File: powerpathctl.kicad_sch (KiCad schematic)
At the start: 11 parts, among them J10 Conn_01x06_Male, J11 Conn_01x06_Male_BAT_data, J8 Conn_01x03_Male_BAT_PWR_IN_NU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, J9 Conn_01x03_Male_BAT_PWR, Q1 SI7149ADP-T1-GE3, U7 LTC4412ES6

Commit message: fixed component number and url for the 5.1kOhm USB pulldown resistors
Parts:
- R20: renamed from R?; footprint (none) -> Resistor_SMD:R_0603_1608Metric; LCSC Part (none) -> C4216
- R21: renamed from R?; footprint (none) -> Resistor_SMD:R_0603_1608Metric; LCSC Part (none) -> C25811
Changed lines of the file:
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@@
   (symbol (lib_id "Device:R") (at 110.7948 81.4832 180) (unit 1)
     (in_bom yes) (on_board yes) (fields_autoplaced)
-    (property "Reference" "R?" (id 0) (at 113.3856 80.2131 0)
+    (property "Reference" "R20" (id 0) (at 113.3856 80.2131 0)
       (effects (font (size 1.27 1.27)) (justify right))
     )
@@
       (effects (font (size 1.27 1.27)) (justify right))
     )
-    (property "Footprint" "" (id 2) (at 112.5728 81.4832 90))
-    (property "Datasheet" "~" (id 3) (at 110.7948 81.4832 0)
+    (property "Footprint" "Resistor_SMD:R_0603_1608Metric" (id 2) (at 112.5728 81.4832 90)
+      (effects (font (size 1.27 1.27)) hide)
+    )
+    (property "Datasheet" "https://datasheet.lcsc.com/lcsc/2206010230_UNI-ROYAL-Uniroyal-Elec-0603WAF3302T5E_C4216.pdf" (id 3) (at 110.7948 81.4832 0)
+      (effects (font (size 1.27 1.27)) hide)
+    )
+    (property "LCSC Part" "C4216" (id 4) (at 110.7948 81.4832 0)
       (effects (font (size 1.27 1.27)) hide)
     )
@@
   (symbol (lib_id "power:GND") (at 110.871 97.4852 0) (unit 1)
     (in_bom yes) (on_board yes) (fields_autoplaced)
-    (property "Reference" "#PWR?" (id 0) (at 110.871 103.8352 0)
+    (property "Reference" "#PWR0131" (id 0) (at 110.871 103.8352 0)
       (effects (font (size 1.27 1.27)) hide)
     )
@@
   (symbol (lib_id "Device:R") (at 110.871 93.0402 0) (unit 1)
     (in_bom yes) (on_board yes) (fields_autoplaced)
-    (property "Reference" "R?" (id 0) (at 113.5126 91.7701 0)
+    (property "Reference" "R21" (id 0) (at 113.5126 91.7701 0)
       (effects (font (size 1.27 1.27)) (justify left))
     )
@@
       (effects (font (size 1.27 1.27)) (justify left))
     )
-    (property "Footprint" "" (id 2) (at 109.093 93.0402 90))
-    (property "Datasheet" "~" (id 3) (at 110.871 93.0402 0)
-      (effects (font (size 1.27 1.27)) hide)
-    )
+    (property "Footprint" "Resistor_SMD:R_0603_1608Metric" (id 2) (at 109.093 93.0402 90)
+      (effects (font (size 1.27 1.27)) hide)
+    )
+    (property "Datasheet" "https://datasheet.lcsc.com/lcsc/2206010045_UNI-ROYAL-Uniroyal-Elec-0603WAF2003T5E_C25811.pdf" (id 3) (at 110.871 93.0402 0)
+      (effects (font (size 1.27 1.27)) hide)
+    )
+    (property "LCSC Part" "C25811" (id 4) (at 110.871 93.0402 0)
+      (effects (font (size 1.27 1.27)) hide)
+    )

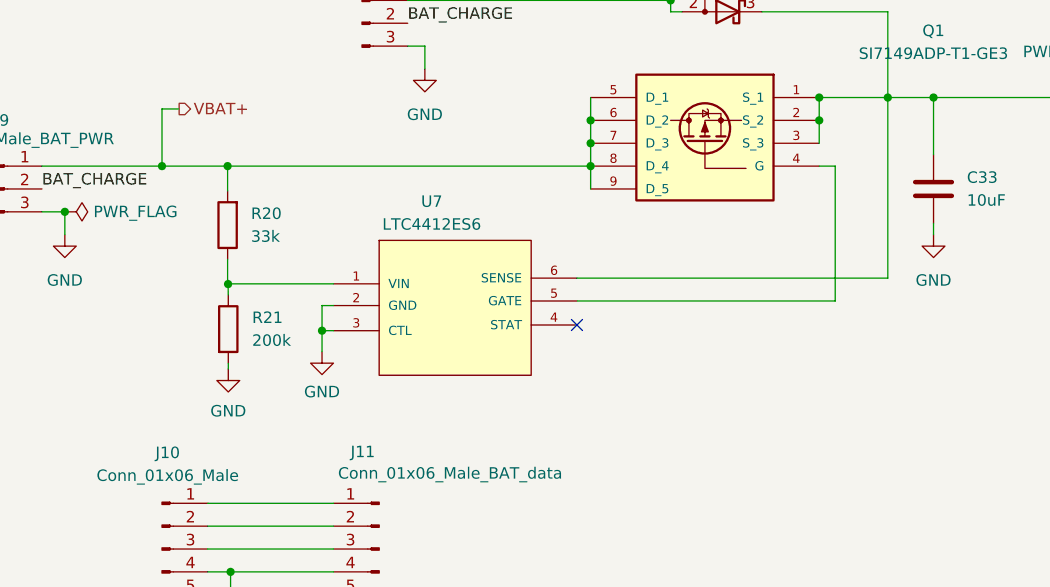
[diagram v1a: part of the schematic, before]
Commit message: updated pcb from schematics, rerouted M1 enc GND and VCC, placed powerpathctl voltage divider
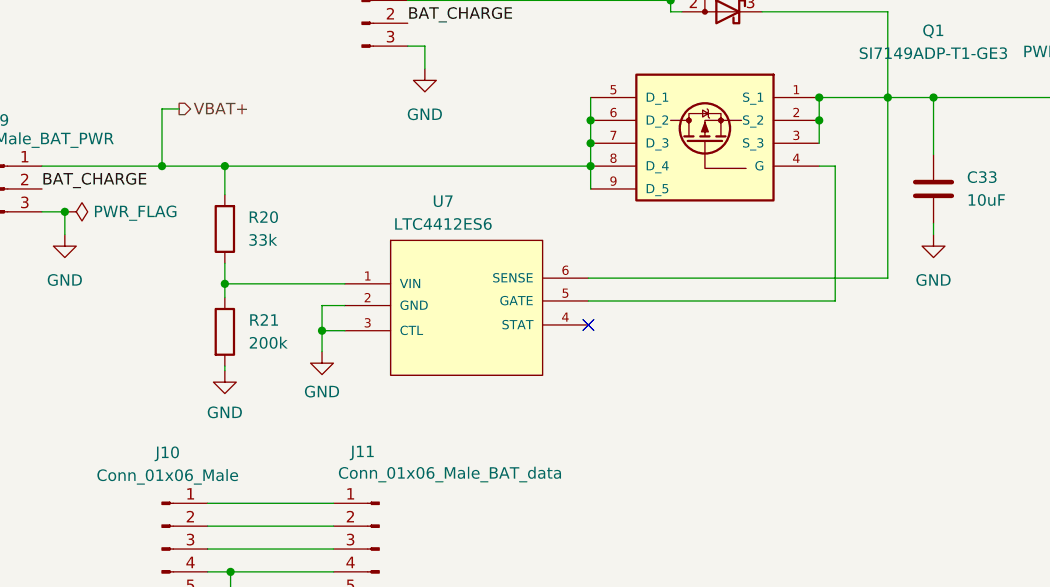
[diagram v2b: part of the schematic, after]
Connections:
- net at R20.1, U7.1 (VIN): now also R21.1
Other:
- moved on the sheet: R20, U7
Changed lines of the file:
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@@
   (junction (at 203.835 67.31) (diameter 0) (color 0 0 0 0)
   )
-  (junction (at 110.7948 74.93) (diameter 0) (color 0 0 0 0)
+  (junction (at 110.49 74.93) (diameter 0) (color 0 0 0 0)
   )
   (junction (at 151.13 74.93) (diameter 0) (color 0 0 0 0)
@@
   (junction (at 103.505 74.93) (diameter 0) (color 0 0 0 0)
   )
+  (junction (at 110.49 88.011) (diameter 0) (color 0 0 0 0)
+  )
   (junction (at 92.71 80.01) (diameter 0) (color 0 0 0 0)
   )
   (junction (at 151.13 72.39) (diameter 0) (color 0 0 0 0)
   )
-  (junction (at 110.8456 88.0364) (diameter 0) (color 0 0 0 0)
-  )
   (junction (at 184.15 67.31) (diameter 0) (color 0 0 0 0)
   )
-  (no_connect (at 149.606 92.583))
+  (no_connect (at 150.876 92.583))
   (wire (pts (xy 132.715 61.595) (xy 132.715 64.135))
     (stroke (width 0) (type default) (color 0 0 0 0))
   )
-  (wire (pts (xy 110.7948 74.93) (xy 151.13 74.93))
+  (wire (pts (xy 110.49 74.93) (xy 151.13 74.93))
     (stroke (width 0) (type default) (color 0 0 0 0))
   )
@@
     (stroke (width 0) (type default) (color 0 0 0 0))
   )
+  (wire (pts (xy 110.49 88.011) (xy 110.49 89.535))
+    (stroke (width 0) (type default) (color 0 0 0 0))
+  )
   (wire (pts (xy 108.585 117.475) (xy 122.555 117.475))
     (stroke (width 0) (type default) (color 0 0 0 0))
@@
     (stroke (width 0) (type default) (color 0 0 0 0))
   )
+  (wire (pts (xy 110.49 88.011) (xy 123.825 88.011))
+    (stroke (width 0) (type default) (color 0 0 0 0))
+  )
   (wire (pts (xy 121.285 90.424) (xy 121.285 93.218))
     (stroke (width 0) (type default) (color 0 0 0 0))
@@
     (stroke (width 0) (type default) (color 0 0 0 0))
   )
-  (wire (pts (xy 149.606 89.916) (xy 178.308 89.916))
-    (stroke (width 0) (type default) (color 0 0 0 0))
-  )
-  (wire (pts (xy 121.285 93.218) (xy 122.555 93.218))
+  (wire (pts (xy 150.876 89.916) (xy 178.308 89.916))
+    (stroke (width 0) (type default) (color 0 0 0 0))
+  )
+  (wire (pts (xy 121.285 93.218) (xy 123.825 93.218))
     (stroke (width 0) (type default) (color 0 0 0 0))
   )
@@
     (stroke (width 0) (type default) (color 0 0 0 0))
   )
-  (wire (pts (xy 110.871 96.8502) (xy 110.871 97.4852))
+  (wire (pts (xy 110.49 97.155) (xy 110.49 97.663))
     (stroke (width 0) (type default) (color 0 0 0 0))
   )
@@
     (stroke (width 0) (type default) (color 0 0 0 0))
   )
-  (wire (pts (xy 122.555 90.424) (xy 121.285 90.424))
+  (wire (pts (xy 123.825 90.424) (xy 121.285 90.424))
     (stroke (width 0) (type default) (color 0 0 0 0))
   )
@@
     (stroke (width 0) (type default) (color 0 0 0 0))
   )
-  (wire (pts (xy 110.871 89.2302) (xy 110.8456 88.0364))
-    (stroke (width 0) (type default) (color 0 0 0 0))
-  )
   (wire (pts (xy 111.125 130.175) (xy 113.03 130.175))
     (stroke (width 0) (type default) (color 0 0 0 0))
@@
     (stroke (width 0) (type default) (color 0 0 0 0))
   )
-  (wire (pts (xy 149.606 87.376) (xy 184.15 87.376))
+  (wire (pts (xy 150.876 87.376) (xy 184.15 87.376))
     (stroke (width 0) (type default) (color 0 0 0 0))
   )
@@
     (stroke (width 0) (type default) (color 0 0 0 0))
   )
-  (wire (pts (xy 103.505 74.93) (xy 110.7948 74.93))
+  (wire (pts (xy 103.505 74.93) (xy 110.49 74.93))
     (stroke (width 0) (type default) (color 0 0 0 0))
   )
@@
     (stroke (width 0) (type default) (color 0 0 0 0))
   )
-  (wire (pts (xy 110.7948 74.93) (xy 110.7948 77.6732))
+  (wire (pts (xy 110.49 74.93) (xy 110.49 78.105))
     (stroke (width 0) (type default) (color 0 0 0 0))
   )
@@
     (stroke (width 0) (type default) (color 0 0 0 0))
   )
-  (wire (pts (xy 110.7948 85.2932) (xy 110.7948 88.011))
-    (stroke (width 0) (type default) (color 0 0 0 0))
-  )
   (wire (pts (xy 111.125 120.015) (xy 111.125 130.175))
     (stroke (width 0) (type default) (color 0 0 0 0))
   )
-  (wire (pts (xy 110.7948 88.011) (xy 122.555 88.011))
+  (wire (pts (xy 110.49 85.725) (xy 110.49 88.011))
     (stroke (width 0) (type default) (color 0 0 0 0))
   )
@@
     (pin "3")
   )
-  (symbol (lib_id "Device:R") (at 110.7948 81.4832 180) (unit 1)
-    (in_bom yes) (on_board yes) (fields_autoplaced)
-    (property "Reference" "R20" (id 0) (at 113.3856 80.2131 0)
+  (symbol (lib_id "Device:R") (at 110.49 81.915 180) (unit 1)
+    (in_bom yes) (on_board yes) (fields_autoplaced)
+    (property "Reference" "R20" (id 0) (at 113.0808 80.6449 0)
       (effects (font (size 1.27 1.27)) (justify right))
     )
-    (property "Value" "33k" (id 1) (at 113.3856 82.7531 0)
+    (property "Value" "33k" (id 1) (at 113.0808 83.1849 0)
       (effects (font (size 1.27 1.27)) (justify right))
     )
-    (property "Footprint" "Resistor_SMD:R_0603_1608Metric" (id 2) (at 112.5728 81.4832 90)
-      (effects (font (size 1.27 1.27)) hide)
-    )
-    (property "Datasheet" "https://datasheet.lcsc.com/lcsc/2206010230_UNI-ROYAL-Uniroyal-Elec-0603WAF3302T5E_C4216.pdf" (id 3) (at 110.7948 81.4832 0)
-      (effects (font (size 1.27 1.27)) hide)
-    )
-    (property "LCSC Part" "C4216" (id 4) (at 110.7948 81.4832 0)
+    (property "Footprint" "Resistor_SMD:R_0603_1608Metric" (id 2) (at 112.268 81.915 90)
+      (effects (font (size 1.27 1.27)) hide)
+    )
+    (property "Datasheet" "https://datasheet.lcsc.com/lcsc/2206010230_UNI-ROYAL-Uniroyal-Elec-0603WAF3302T5E_C4216.pdf" (id 3) (at 110.49 81.915 0)
+      (effects (font (size 1.27 1.27)) hide)
+    )
+    (property "LCSC Part" "C4216" (id 4) (at 110.49 81.915 0)
       (effects (font (size 1.27 1.27)) hide)
     )
@@
     (pin "1")
   )
-  (symbol (lib_id "LTC4412ES6:LTC4412ES6") (at 127.635 83.185 0) (unit 1)
-    (in_bom yes) (on_board yes)
-    (property "Reference" "U7" (id 0) (at 133.477 78.867 0))
-    (property "Value" "LTC4412ES6" (id 1) (at 133.477 81.407 0))
-    (property "Footprint" "Robotont:TSOT-23_S6" (id 2) (at 120.015 88.011 0)
-      (effects (font (size 1.27 1.27)) (justify bottom) hide)
-    )
-    (property "Datasheet" "https://www.analog.com/media/en/technical-documentation/data-sheets/ltc4412.pdf" (id 3) (at 120.015 88.011 0)
-      (effects (font (size 1.27 1.27)) hide)
-    )
-    (property "VENDOR" "Linear Technology" (id 4) (at 120.015 88.011 0)
-      (effects (font (size 1.27 1.27)) (justify bottom) hide)
-    )
-    (property "MANUFACTURER_PART_NUMBER" "ltc4412es6" (id 5) (at 120.015 88.011 0)
-      (effects (font (size 1.27 1.27)) (justify bottom) hide)
-    )
-    (property "LCSC Part" "C514442" (id 6) (at 127.635 83.185 0)
+  (symbol (lib_id "LTC4412ES6:LTC4412ES6") (at 128.905 83.185 0) (unit 1)
+    (in_bom yes) (on_board yes)
+    (property "Reference" "U7" (id 0) (at 134.747 78.867 0))
+    (property "Value" "LTC4412ES6" (id 1) (at 134.747 81.407 0))
+    (property "Footprint" "Robotont:TSOT-23_S6" (id 2) (at 121.285 88.011 0)
+      (effects (font (size 1.27 1.27)) (justify bottom) hide)
+    )
+    (property "Datasheet" "https://www.analog.com/media/en/technical-documentation/data-sheets/ltc4412.pdf" (id 3) (at 121.285 88.011 0)
+      (effects (font (size 1.27 1.27)) hide)
+    )
+    (property "VENDOR" "Linear Technology" (id 4) (at 121.285 88.011 0)
+      (effects (font (size 1.27 1.27)) (justify bottom) hide)
+    )
+    (property "MANUFACTURER_PART_NUMBER" "ltc4412es6" (id 5) (at 121.285 88.011 0)
+      (effects (font (size 1.27 1.27)) (justify bottom) hide)
+    )
+    (property "LCSC Part" "C514442" (id 6) (at 128.905 83.185 0)
       (effects (font (size 1.27 1.27)) hide)
     )
@@
     (pin "2")
   )
-  (symbol (lib_id "power:GND") (at 110.871 97.4852 0) (unit 1)
-    (in_bom yes) (on_board yes) (fields_autoplaced)
-    (property "Reference" "#PWR0131" (id 0) (at 110.871 103.8352 0)
-      (effects (font (size 1.27 1.27)) hide)
-    )
-    (property "Value" "GND" (id 1) (at 110.871 102.1588 0))
-    (property "Footprint" "" (id 2) (at 110.871 97.4852 0)
-      (effects (font (size 1.27 1.27)) hide)
-    )
-    (property "Datasheet" "" (id 3) (at 110.871 97.4852 0)
+  (symbol (lib_id "power:GND") (at 110.49 97.663 0) (unit 1)
+    (in_bom yes) (on_board yes) (fields_autoplaced)
+    (property "Reference" "#PWR0131" (id 0) (at 110.49 104.013 0)
+      (effects (font (size 1.27 1.27)) hide)
+    )
+    (property "Value" "GND" (id 1) (at 110.49 102.3366 0))
+    (property "Footprint" "" (id 2) (at 110.49 97.663 0)
+      (effects (font (size 1.27 1.27)) hide)
+    )
+    (property "Datasheet" "" (id 3) (at 110.49 97.663 0)
       (effects (font (size 1.27 1.27)) hide)
     )
@@
     (pin "9")
   )
-  (symbol (lib_id "Device:R") (at 110.871 93.0402 0) (unit 1)
-    (in_bom yes) (on_board yes) (fields_autoplaced)
-    (property "Reference" "R21" (id 0) (at 113.5126 91.7701 0)
+  (symbol (lib_id "Device:R") (at 110.49 93.345 0) (unit 1)
+    (in_bom yes) (on_board yes) (fields_autoplaced)
+    (property "Reference" "R21" (id 0) (at 113.1316 92.0749 0)
       (effects (font (size 1.27 1.27)) (justify left))
     )
-    (property "Value" "200k" (id 1) (at 113.5126 94.3101 0)
+    (property "Value" "200k" (id 1) (at 113.1316 94.6149 0)
       (effects (font (size 1.27 1.27)) (justify left))
     )
-    (property "Footprint" "Resistor_SMD:R_0603_1608Metric" (id 2) (at 109.093 93.0402 90)
-      (effects (font (size 1.27 1.27)) hide)
-    )
-    (property "Datasheet" "https://datasheet.lcsc.com/lcsc/2206010045_UNI-ROYAL-Uniroyal-Elec-0603WAF2003T5E_C25811.pdf" (id 3) (at 110.871 93.0402 0)
-      (effects (font (size 1.27 1.27)) hide)
-    )
-    (property "LCSC Part" "C25811" (id 4) (at 110.871 93.0402 0)
-      (effects (font (size 1.27 1.27)) hide)
-    )
+    (property "Footprint" "Resistor_SMD:R_0603_1608Metric" (id 2) (at 108.712 93.345 90)
+      (effects (font (size 1.27 1.27)) hide)
+    )
+    (property "Datasheet" "https://datasheet.lcsc.com/lcsc/2206010045_UNI-ROYAL-Uniroyal-Elec-0603WAF2003T5E_C25811.pdf" (id 3) (at 110.49 93.345 0)
+      (effects (font (size 1.27 1.27)) hide)
+    )
+    (property "LCSC Part" "C25811" (id 4) (at 110.49 93.345 0)
+      (effects (font (size 1.27 1.27)) hide)
+    )
